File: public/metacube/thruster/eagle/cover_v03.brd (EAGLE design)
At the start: 30 x 49.2 mm, 0 parts

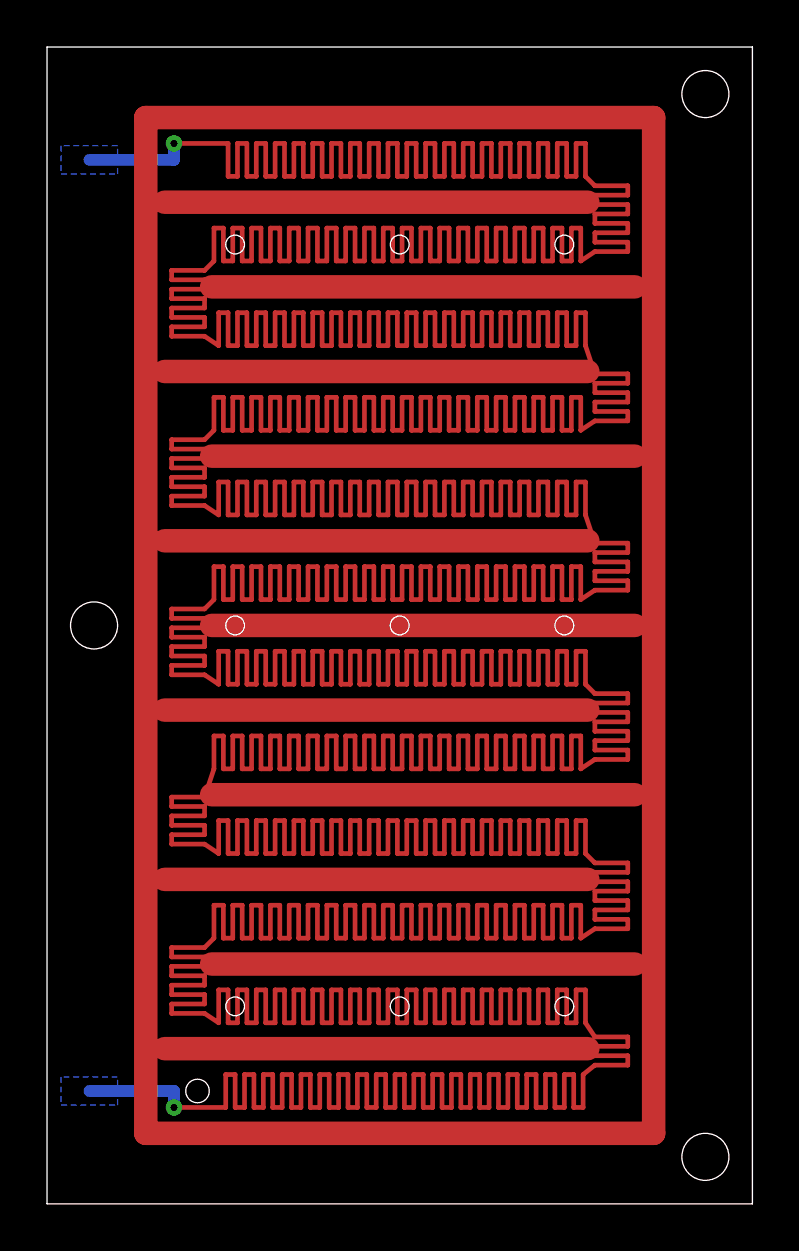
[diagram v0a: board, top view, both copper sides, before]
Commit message: 추력기: 히터 U턴 코너 채움(1121 mm·8.5 Ω/면·직렬 16.9 Ω·30 W@24 V), EAGLE·뷰어·도면·예측표·치수표 갱신
Co-Authored-By: Claude Fable 5 <noreply@anthropic.com>
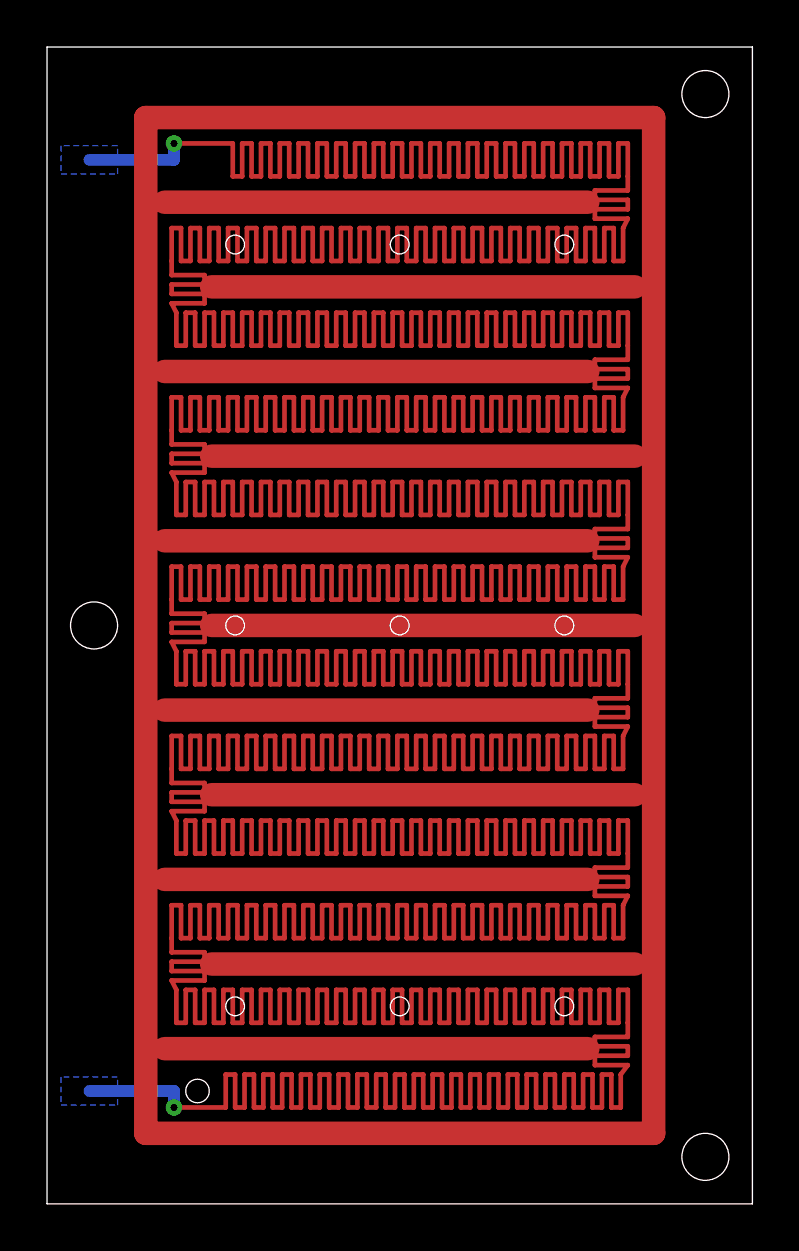
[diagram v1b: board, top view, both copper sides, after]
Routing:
- net HTR: track 1021.0 -> 1131.7 mm
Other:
- board text added: "heater transverse zigzag 0.20/0.20 in 1.6 band inside channel, L=1123 mm, ~8.5 Ohm @1.4mOhm/sq+0.6"
- board text removed: "heater transverse zigzag 0.20/0.20 in 1.6 band inside channel, L=1012 mm, ~7.7 Ohm @1.4mOhm/sq+0.6"

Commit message: 추력기 설계변경(댓글 김성현): 커버 랜드-히터 간섭 제거(랜드 끝 0.3 여유), 코어 슬롯 Milling→Dimension 폐곡선; EAGLE·뷰어·도면 갱신
Co-Authored-By: Claude Fable 5 <noreply@anthropic.com>
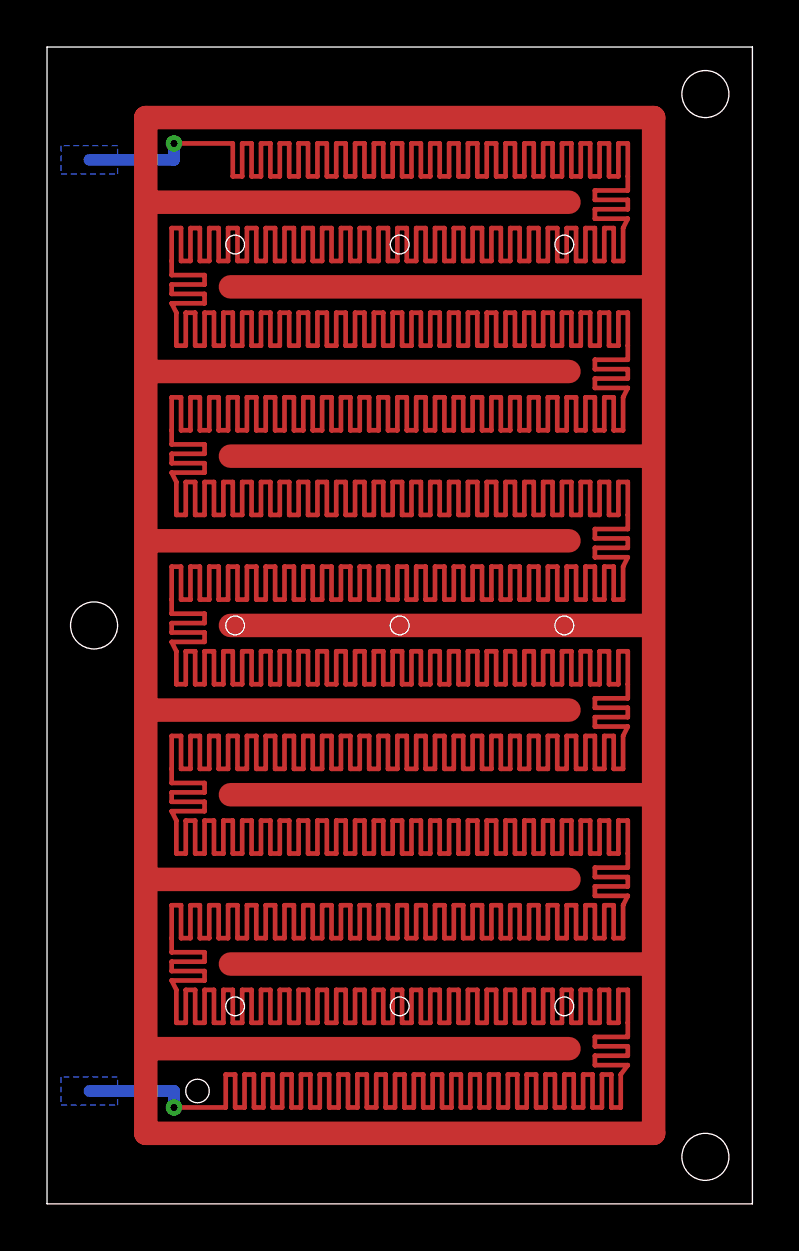
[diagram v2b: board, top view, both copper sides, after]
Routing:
- net LAND: track 327.6 -> 322.1 mm

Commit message: 추력기: 라우터 R1.0 코너·슬롯 끝 라운드에 맞춰 히터 클립·비아/포트 이동(밀봉선 간섭 제거), 추진제 데이터 엑셀(정의·출처 시트) 다운로드 추가
Co-Authored-By: Claude Fable 5 <noreply@anthropic.com>
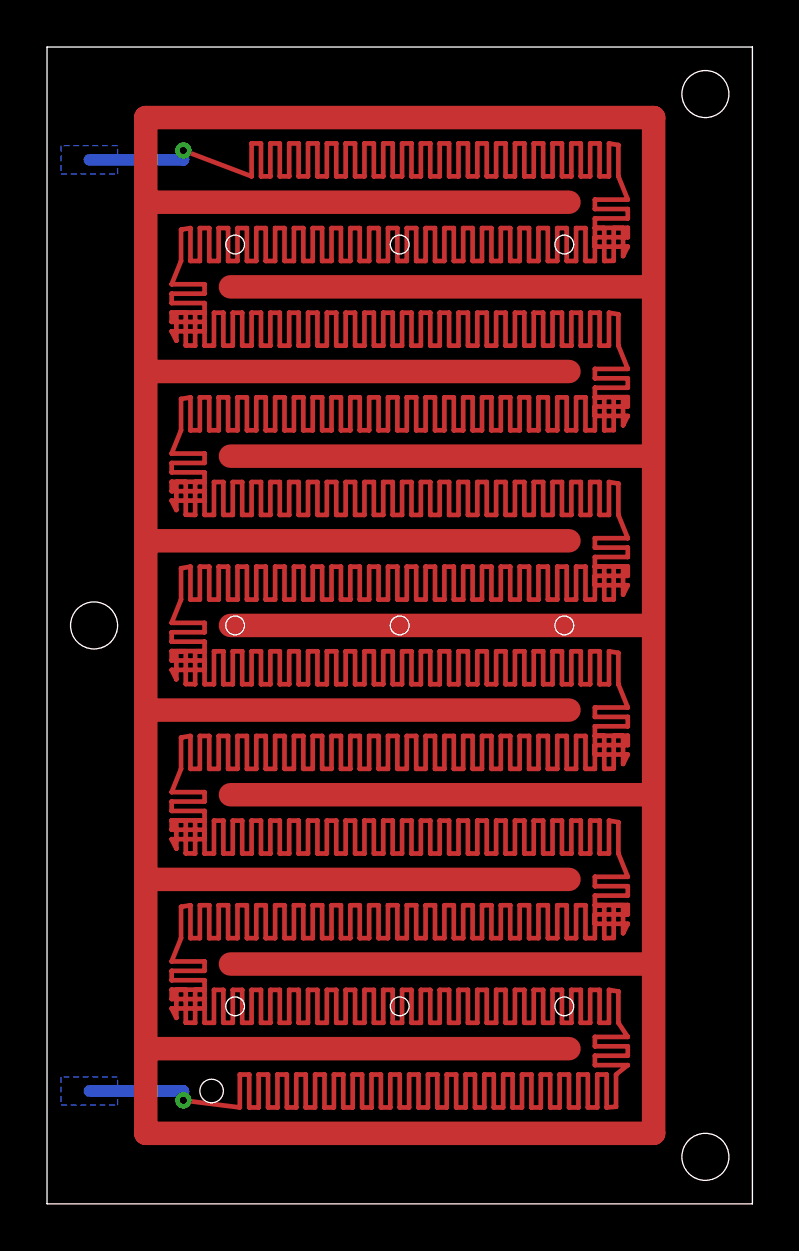
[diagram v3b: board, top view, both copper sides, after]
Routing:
- net HTR: track 1131.7 -> 1143.7 mm
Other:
- board text added: "heater transverse zigzag 0.20/0.20 in 1.6 band inside channel, L=1135 mm, ~8.5 Ohm @1.4mOhm/sq+0.6"
- board text removed: "heater transverse zigzag 0.20/0.20 in 1.6 band inside channel, L=1123 mm, ~8.5 Ohm @1.4mOhm/sq+0.6"

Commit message: 추력기: 켈빈 센스 패드, 입구 리스트릭터 φ0.15, CHF 문구 삭제·벽온/콜드스타트 밴드 정정, 계측·밀봉 리스크 갱신, 히터 17.1 Ω
Co-Authored-By: Claude Fable 5 <noreply@anthropic.com>
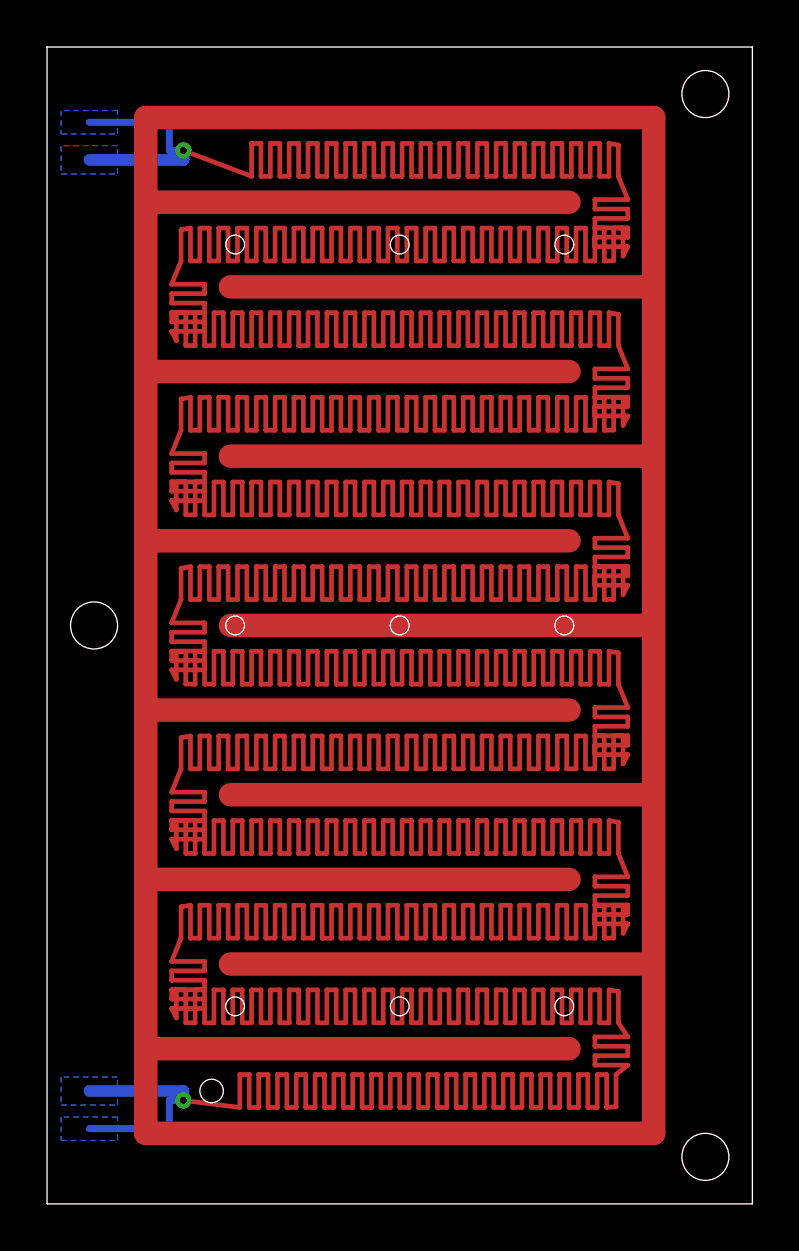
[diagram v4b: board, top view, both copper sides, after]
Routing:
- net HTR: track 1143.7 -> 1154.1 mm
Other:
- board text added: "2 vias phi0.3 (pad 0.7) at channel start/end = INSIDE sealed cavity -> MUST be solder-filled at reflow. Outer face (L16): force pads F at y 4.8/44.4 + Kelvin sense pads S at y 3.2/46.0 (4-wire heater R(T)). SAME PART for top and bottom cover (flip about x-axis)."
- board text removed: "2 vias phi0.3 (pad 0.7) at channel start/end = INSIDE sealed cavity -> MUST be solder-filled at reflow. Pads on OUTER face (L16). SAME PART for top and bottom cover (flip about x-axis)."
